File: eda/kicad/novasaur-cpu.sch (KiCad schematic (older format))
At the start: 29 parts, among them U14 27C020, U15 AS6C4008, U16 74F574, U17 74F163, U18 74F163, U19 74F541, U20 74F574, U21 74F574, U22 74F257, U23 74F574, U24 74F574, U25 74F574, U26 74F574, U27 74F244, U27 74F541

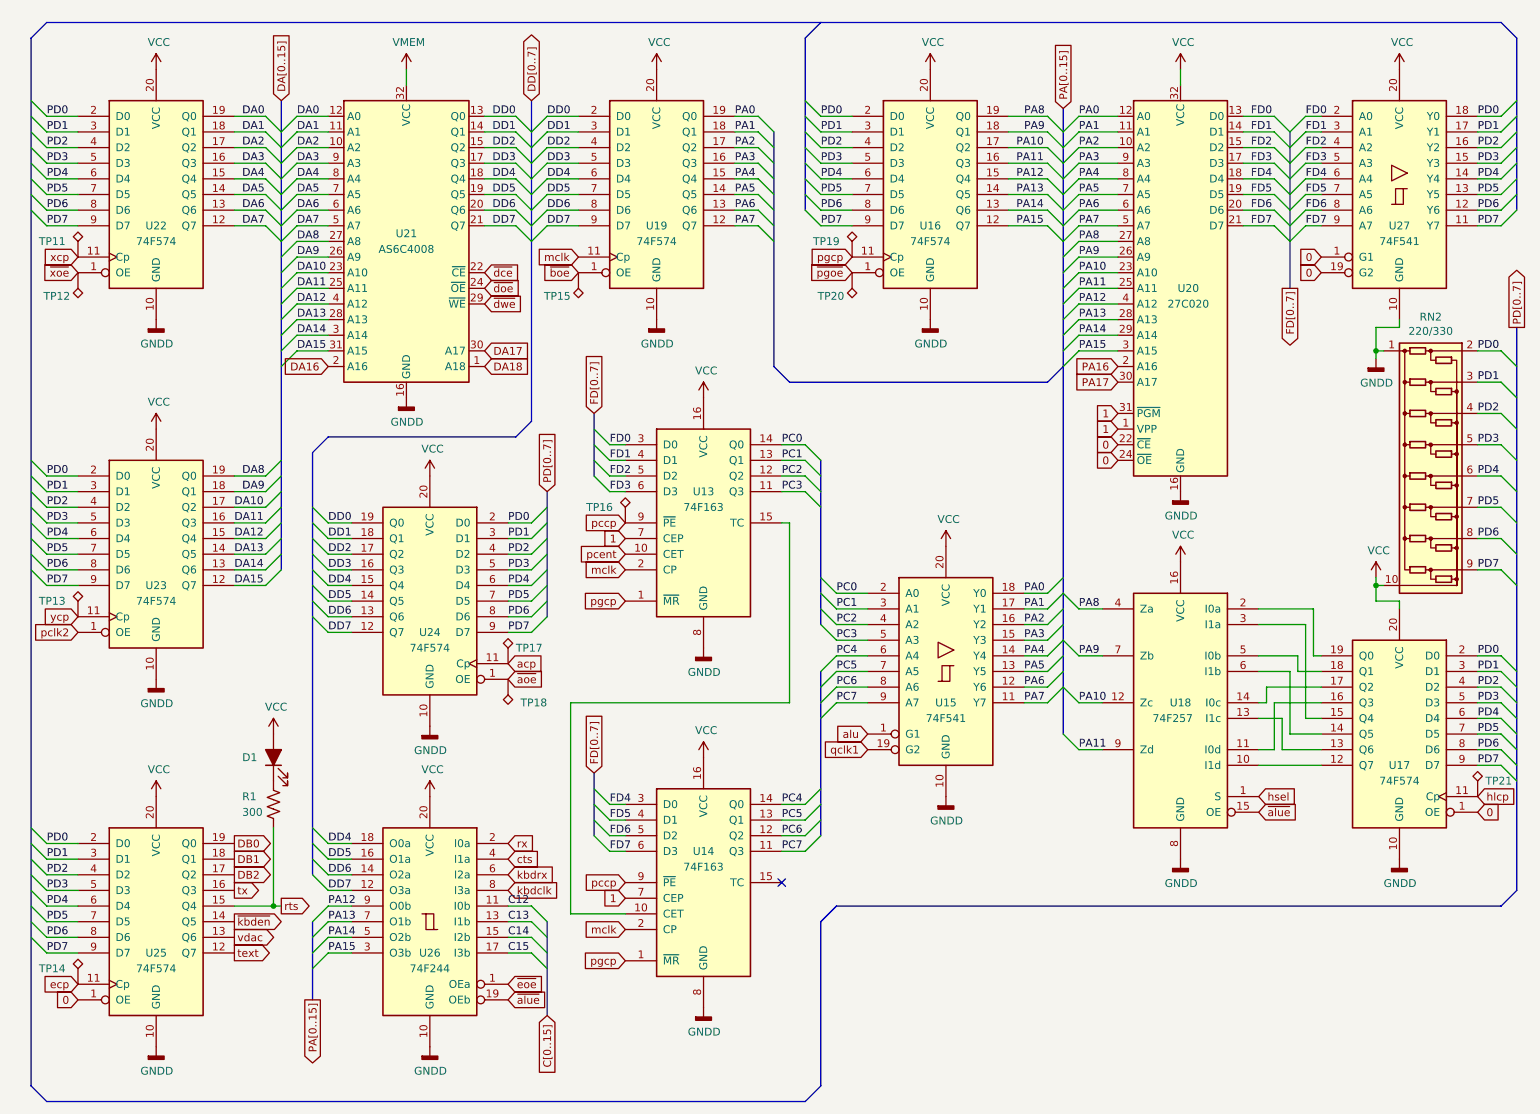
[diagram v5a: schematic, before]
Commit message: annotate registers
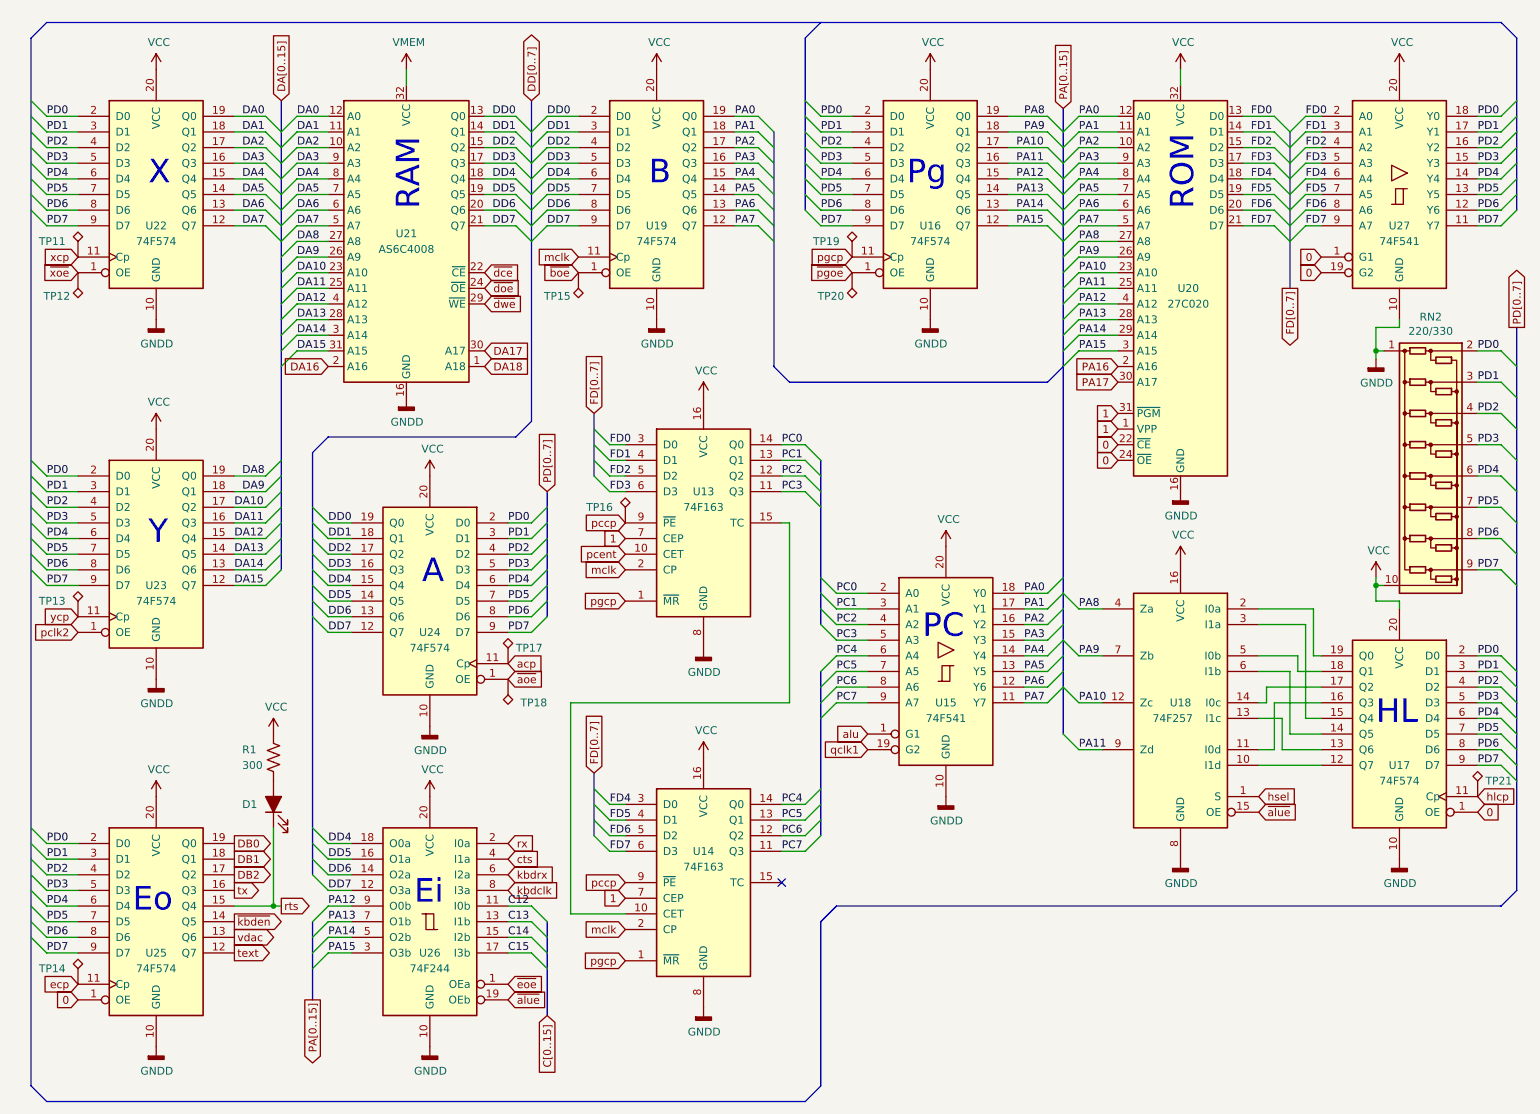
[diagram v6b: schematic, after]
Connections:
- net VCC: now also R1.1; no longer D1.2 (A)
- net rts: now also D1.1 (K); no longer R1.2
- new net: D1.2 (A), R1.2
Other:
- note added: "A"
- note added: "B"
- note added: "Ei"
- note added: "Eo"
- note added: "HL"
- note added: "PC"
- note added: "Pg"
- note added: "RAM"
- note added: "ROM"
- note added: "X"
- note added: "Y"
- moved on the sheet: D1, R1
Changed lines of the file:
@@
 Sheet 2 4
 Title "Central Processing Unit"
-Date "2021-10-20"
+Date "2021-11-20"
 Rev "1.10"
 Comp ""
@@
 L Device:LED_ALT D?
 U 1 1 5EE6CB39
-P 2300 5500
+P 2300 5800
 AR Path="/5DAA19D5/5EE6CB39" Ref="D?"  Part="1"
 AR Path="/5DAA5CD8/5D99DA9F/5EE6CB39" Ref="D?"  Part="1"
 AR Path="/5DA1E9BA/5EE6CB39" Ref="D1"  Part="1"
 AR Path="/5EE6CB39" Ref="D?"  Part="1"
-F 0 "D1" V 2300 5700 50  0000 R CNN
-F 1 "LTL-10223W" V 2248 5383 50  0001 R CNN
-F 2 "LED_THT:LED_D5.0mm_Horizontal_O1.27mm_Z3.0mm_Clear" H 2300 5500 50  0001 C CNN
-F 3 "~" H 2300 5500 50  0001 C CNN
-	1    2300 5500
+F 0 "D1" V 2300 6000 50  0000 R CNN
+F 1 "LTL-10223W" V 2248 5683 50  0001 R CNN
+F 2 "LED_THT:LED_D5.0mm_Horizontal_O1.27mm_Z3.0mm_Clear" H 2300 5800 50  0001 C CNN
+F 3 "~" H 2300 5800 50  0001 C CNN
+	1    2300 5800
 	0    -1   -1   0
 $EndComp
@@
 L Device:R_US R?
 U 1 1 5EE6CB33
-P 2300 5800
+P 2300 5500
 AR Path="/62D13D9D/5EE6CB33" Ref="R?"  Part="1"
 AR Path="/5DAA19D5/5EE6CB33" Ref="R?"  Part="1"
@@
 AR Path="/5DA1E9BA/5EE6CB33" Ref="R1"  Part="1"
 AR Path="/5EE6CB33" Ref="R?"  Part="1"
-F 0 "R1" H 2100 5850 50  0000 L CNN
-F 1 "300" H 2100 5750 50  0000 L CNN
-F 2 "Resistor_THT:R_Axial_DIN0204_L3.6mm_D1.6mm_P7.62mm_Horizontal" V 2340 5790 50  0001 C CNN
-F 3 "~" H 2300 5800 50  0001 C CNN
-	1    2300 5800
-	1    0    0    -1
-$EndComp
+F 0 "R1" H 2100 5550 50  0000 L CNN
+F 1 "300" H 2100 5450 50  0000 L CNN
+F 2 "Resistor_THT:R_Axial_DIN0204_L3.6mm_D1.6mm_P7.62mm_Horizontal" V 2340 5490 50  0001 C CNN
+F 3 "~" H 2300 5500 50  0001 C CNN
+	1    2300 5500
+	1    0    0    -1
+$EndComp
+Text Notes 1500 4150 0    150  ~ 0
+Y
+Text Notes 1400 6500 0    150  ~ 0
+Eo
+Text Notes 3200 6450 0    150  ~ 0
+Ei
+Text Notes 3250 4400 0    150  ~ 0
+A
+Text Notes 1500 1850 0    150  ~ 0
+X
+Text Notes 3250 2000 1    150  ~ 0
+RAM
+Text Notes 4700 1850 0    150  ~ 0
+B
+Text Notes 6350 1850 0    150  ~ 0
+Pg
+Text Notes 6450 4750 0    150  ~ 0
+PC
+Text Notes 8200 2000 1    150  ~ 0
+ROM
+Text Notes 9350 5300 0    150  ~ 0
+HL
 Wire Bus Line
 	850  800  10150 800

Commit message: Shipped Rev. A design
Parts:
- R1: value 300 -> 220
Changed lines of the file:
@@
 Sheet 2 4
 Title "Central Processing Unit"
-Date "2021-11-20"
+Date "2021-12-27"
 Rev "1.10"
 Comp ""
@@
 AR Path="/5EE6CB33" Ref="R?"  Part="1"
 F 0 "R1" H 2100 5550 50  0000 L CNN
-F 1 "300" H 2100 5450 50  0000 L CNN
+F 1 "220" H 2100 5450 50  0000 L CNN
 F 2 "Resistor_THT:R_Axial_DIN0204_L3.6mm_D1.6mm_P7.62mm_Horizontal" V 2340 5490 50  0001 C CNN
 F 3 "~" H 2300 5500 50  0001 C CNN
